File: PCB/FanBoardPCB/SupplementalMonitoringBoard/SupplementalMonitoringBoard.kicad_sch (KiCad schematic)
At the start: 6 parts, among them J1 Conn_01x02, U1 ADC101C021CIMK, U2 TLV2372

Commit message: finished PCB
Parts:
- removed J1: Conn_01x02, symbol Connector_Generic:Conn_01x02
- removed R1, R2, R3: R, symbol Device:R
- removed U1: ADC101C021CIMK, Package_TO_SOT_SMD:SOT-23-6, symbol Analog_ADC:ADC101C021CIMK
- removed U2: TLV2372, symbol Amplifier_Operational:TLV2372
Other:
- added sheet Current (current.kicad_sch)
- added sheet Temperature (temperature.kicad_sch)
- added sheet Voltage (voltage.kicad_sch)
- note added: "ADC"
- note added: "Supplemental Monitoring Board"

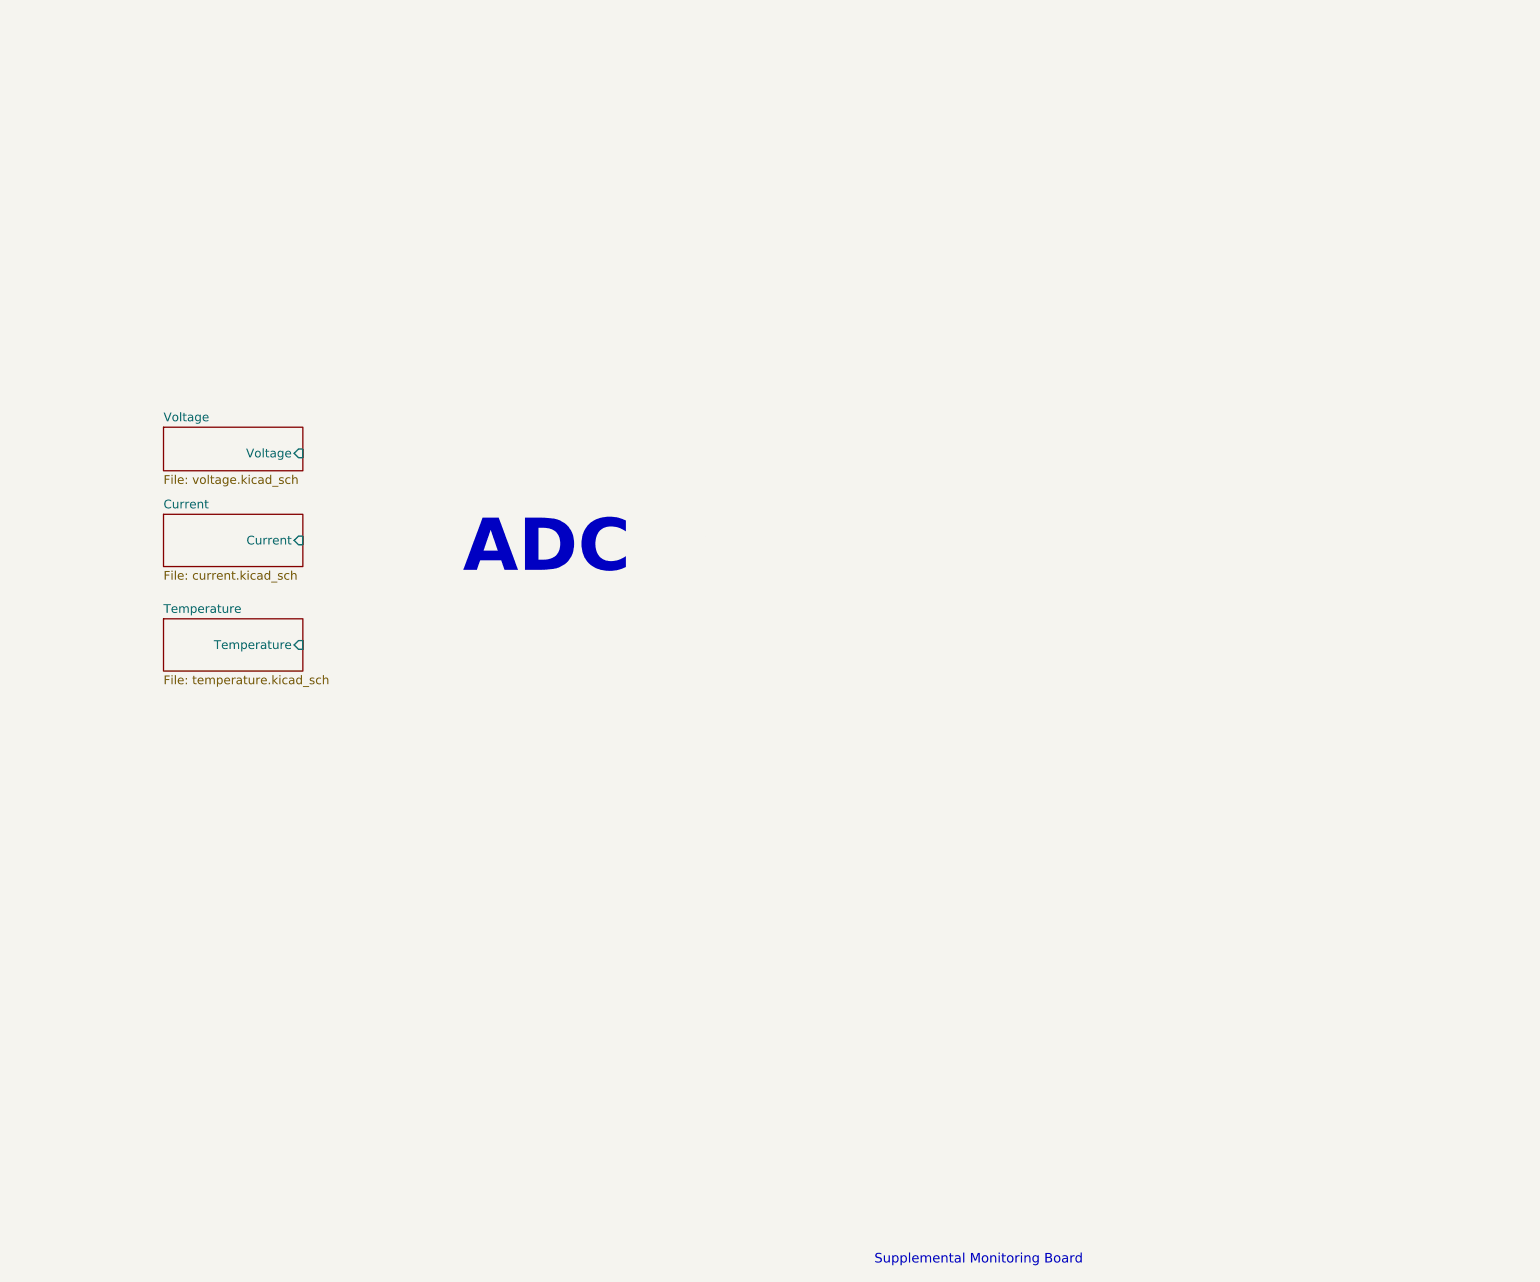
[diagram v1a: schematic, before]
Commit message: Supplemental Monitoring Board
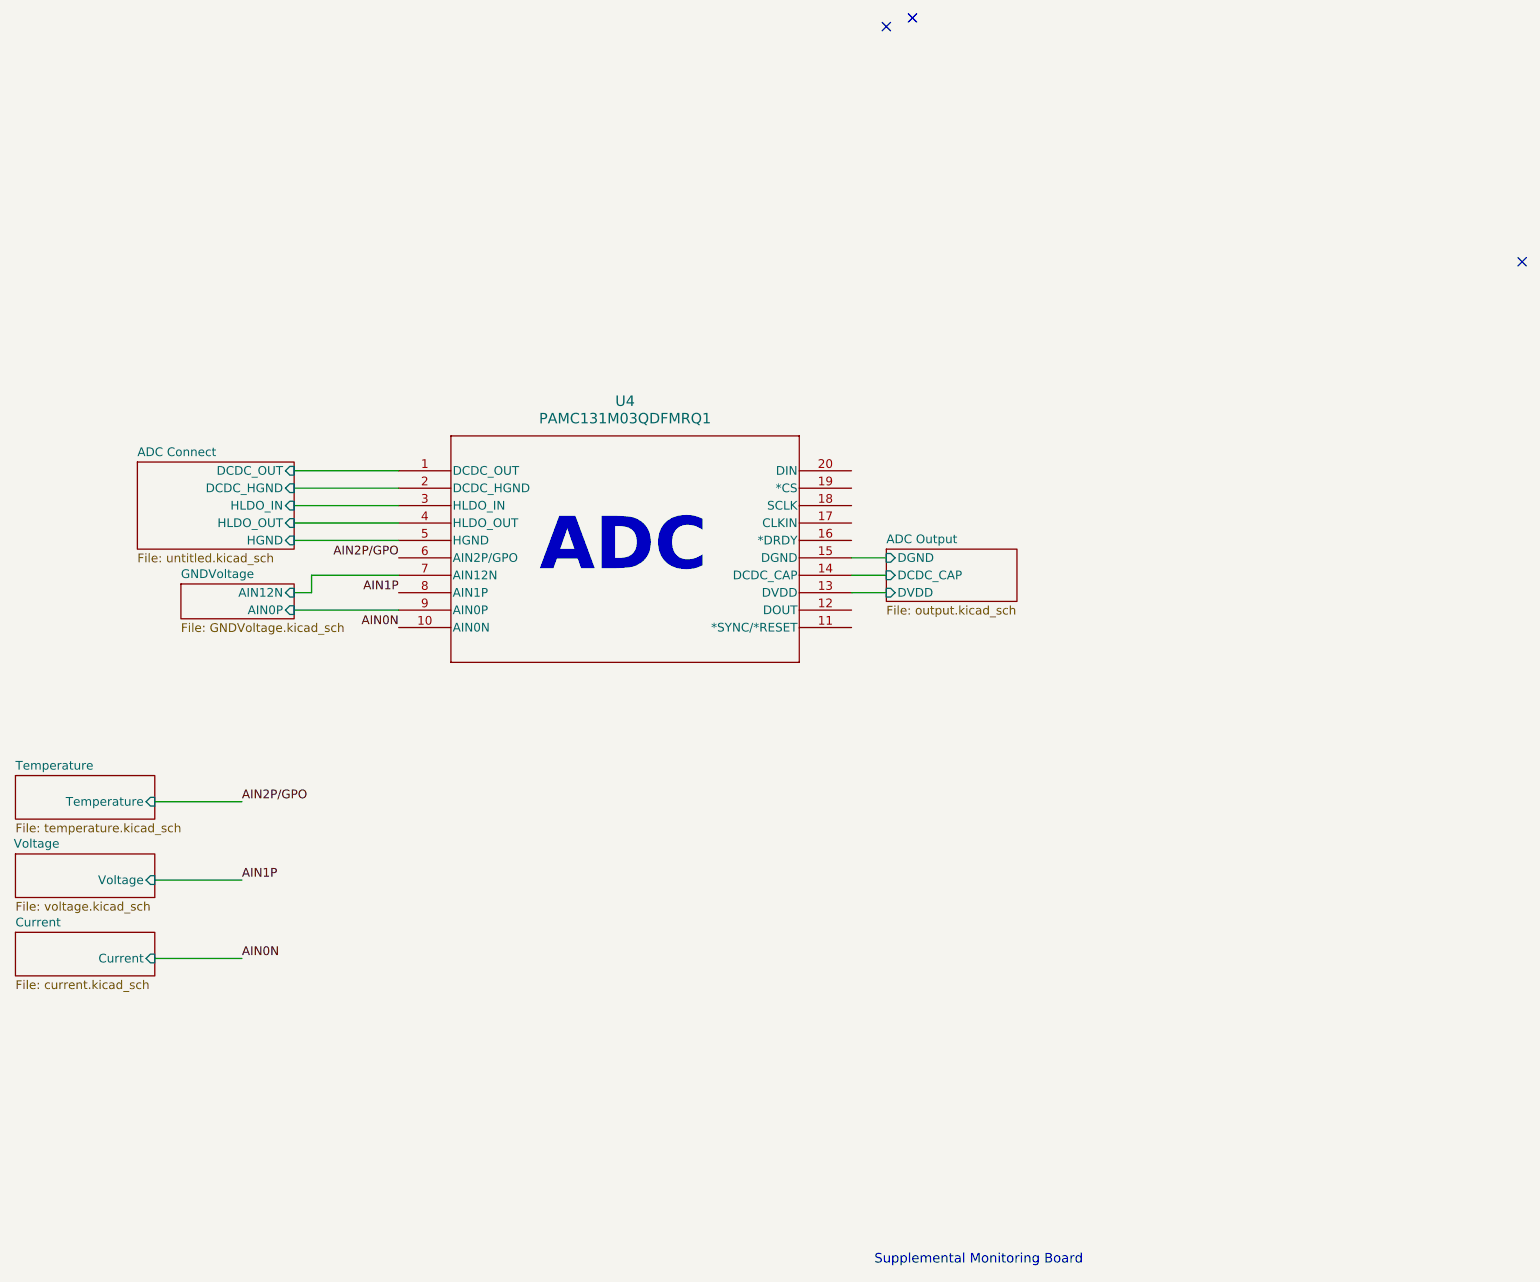
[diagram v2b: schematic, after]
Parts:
- added U4: PAMC131M03QDFMRQ1, ADCfootprints:SOIC20_DFM_TEX, symbol ADC:PAMC131M03QDFMRQ1
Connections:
- new net ADC Connect/DCDC_HGND: U4.2 (DCDC_HGND)
- new net ADC Connect/DCDC_OUT: U4.1 (DCDC_OUT)
- new net ADC Connect/HGND: U4.5 (HGND)
- new net ADC Connect/HLDO_IN: U4.3 (HLDO_IN)
- new net ADC Connect/HLDO_OUT: U4.4 (HLDO_OUT)
- new net ADC Output/DCDC_CAP: U4.14 (DCDC_CAP)
- new net ADC Output/DGND: U4.15 (DGND)
- new net ADC Output/DVDD: U4.13 (DVDD)
- new net AIN0N: U4.10 (AIN0N)
- new net AIN1P: U4.8 (AIN1P)
- new net AIN2P/GPO: U4.6 (AIN2P/GPO)
- new net GNDVoltage/AIN0P: U4.9 (AIN0P)
- new net GNDVoltage/AIN12N: U4.7 (AIN12N)
- no-connect marks 0 -> 3
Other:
- added sheet ADC Connect (untitled.kicad_sch)
- added sheet ADC Output (output.kicad_sch)
- added sheet GNDVoltage (GNDVoltage.kicad_sch)
